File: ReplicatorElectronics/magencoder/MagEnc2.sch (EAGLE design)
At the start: 15 parts, among them IC2 AS5145

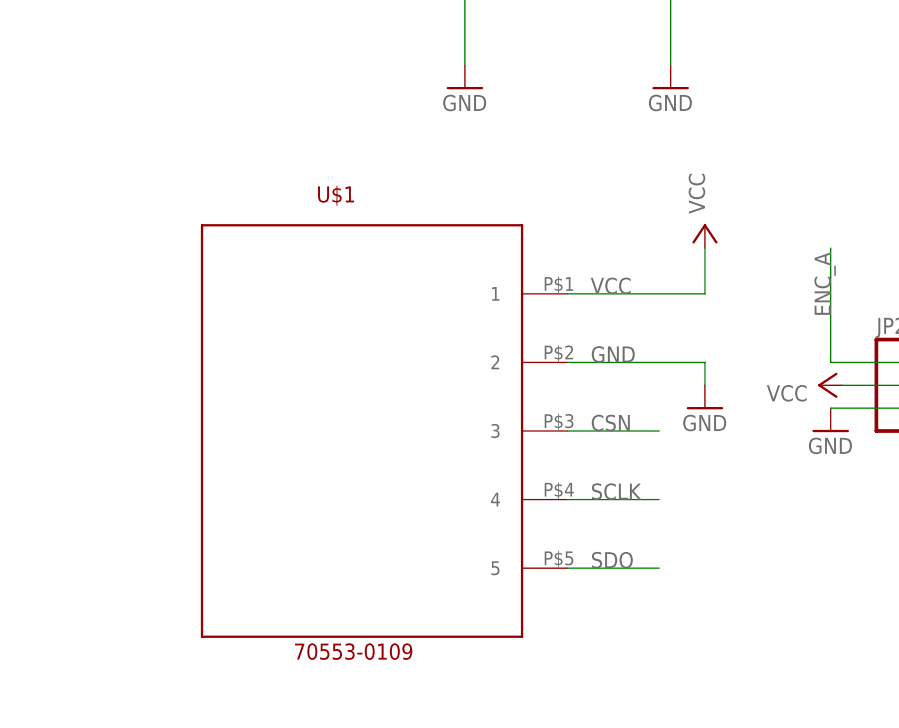
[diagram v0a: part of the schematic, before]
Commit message: 2/23/11: Added Rev. 2 Encoder Board. Fixes disconnect between layout and schematic, Header yet to be placed and routed.
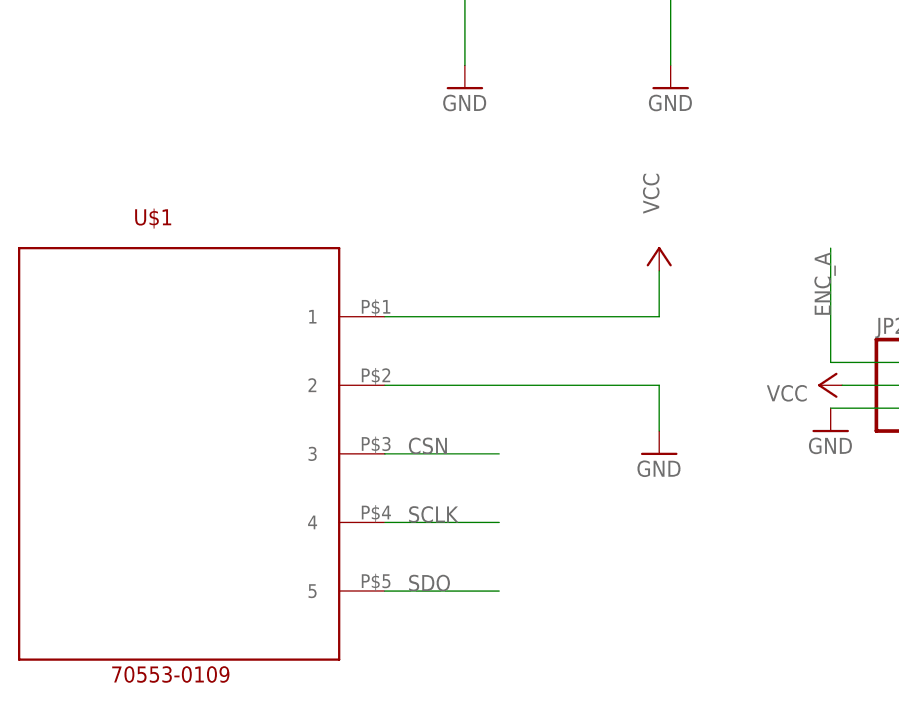
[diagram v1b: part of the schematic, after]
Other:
- moved on the sheet: U$1
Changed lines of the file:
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@@
 <part name="C2" library="rcl" deviceset="C-EU" device="C0805K" value="10uf"/>
 <part name="C4" library="rcl" deviceset="C-EU" device="C0805K" value="10uf"/>
+<part name="U$1" library="70553-0109" deviceset="70553-0106" device=""/>
 <part name="P+2" library="supply1" deviceset="VCC" device=""/>
-<part name="GND1" library="supply1" deviceset="GND" device=""/>
-<part name="U$1" library="70553-0109" deviceset="70553-0106" device=""/>
+<part name="GND7" library="supply1" deviceset="GND" device=""/>
 </parts>
 <sheets>
@@
 <instance part="C2" gate="G$1" x="123.19" y="43.18"/>
 <instance part="C4" gate="G$1" x="138.43" y="43.18"/>
-<instance part="P+2" gate="VCC" x="-17.78" y="2.54" smashed="yes">
-<attribute name="VALUE" x="-17.78" y="3.81" size="1.778" layer="96" rot="R90"/>
+<instance part="U$1" gate="G$1" x="-86.36" y="-40.64"/>
+<instance part="P+2" gate="VCC" x="-22.86" y="0" smashed="yes">
+<attribute name="VALUE" x="-22.86" y="3.81" size="1.778" layer="96" rot="R90"/>
 </instance>
-<instance part="GND1" gate="1" x="-17.78" y="-17.78"/>
-<instance part="U$1" gate="G$1" x="-66.04" y="-38.1"/>
+<instance part="GND7" gate="1" x="-22.86" y="-22.86"/>
 </instances>
 <busses>
@@
 </segment>
 <segment>
-<wire x1="-33.02" y1="-12.7" x2="-17.78" y2="-12.7" width="0.1524" layer="91"/>
-<label x="-30.48" y="-12.7" size="1.778" layer="95"/>
-<pinref part="GND1" gate="1" pin="GND"/>
-<wire x1="-17.78" y1="-12.7" x2="-17.78" y2="-15.24" width="0.1524" layer="91"/>
 <pinref part="U$1" gate="G$1" pin="2"/>
+<pinref part="GND7" gate="1" pin="GND"/>
+<wire x1="-53.34" y1="-15.24" x2="-22.86" y2="-15.24" width="0.1524" layer="91"/>
+<wire x1="-22.86" y1="-15.24" x2="-22.86" y2="-20.32" width="0.1524" layer="91"/>
 </segment>
 <segment>
@@
 </segment>
 <segment>
-<wire x1="-33.02" y1="-5.08" x2="-17.78" y2="-5.08" width="0.1524" layer="91"/>
-<label x="-30.48" y="-5.08" size="1.778" layer="95"/>
+<pinref part="U$1" gate="G$1" pin="1"/>
 <pinref part="P+2" gate="VCC" pin="VCC"/>
-<wire x1="-17.78" y1="-5.08" x2="-17.78" y2="0" width="0.1524" layer="91"/>
-<pinref part="U$1" gate="G$1" pin="1"/>
+<wire x1="-53.34" y1="-7.62" x2="-22.86" y2="-7.62" width="0.1524" layer="91"/>
+<wire x1="-22.86" y1="-7.62" x2="-22.86" y2="-2.54" width="0.1524" layer="91"/>
 </segment>
 </net>
@@
 </segment>
 </net>
+<net name="CSN" class="0">
+<segment>
+<pinref part="IC2" gate="G$1" pin="CSN"/>
+<wire x1="58.42" y1="38.1" x2="66.04" y2="38.1" width="0.1524" layer="91"/>
+<label x="58.42" y="38.1" size="1.778" layer="95"/>
+</segment>
+<segment>
+<pinref part="U$1" gate="G$1" pin="3"/>
+<wire x1="-53.34" y1="-22.86" x2="-40.64" y2="-22.86" width="0.1524" layer="91"/>
+<label x="-50.8" y="-22.86" size="1.778" layer="95"/>
+</segment>
+</net>
 <net name="SCLK" class="0">
 <segment>
@@
 </segment>
 <segment>
-<wire x1="-33.02" y1="-27.94" x2="-22.86" y2="-27.94" width="0.1524" layer="91"/>
-<label x="-30.48" y="-27.94" size="1.778" layer="95"/>
 <pinref part="U$1" gate="G$1" pin="4"/>
+<wire x1="-53.34" y1="-30.48" x2="-40.64" y2="-30.48" width="0.1524" layer="91"/>
+<label x="-50.8" y="-30.48" size="1.778" layer="95"/>
 </segment>
 </net>
@@
 </segment>
 <segment>
-<wire x1="-33.02" y1="-35.56" x2="-22.86" y2="-35.56" width="0.1524" layer="91"/>
-<label x="-30.48" y="-35.56" size="1.778" layer="95"/>
 <pinref part="U$1" gate="G$1" pin="5"/>
-</segment>
-</net>
-<net name="CSN" class="0">
-<segment>
-<pinref part="IC2" gate="G$1" pin="CSN"/>
-<wire x1="58.42" y1="38.1" x2="66.04" y2="38.1" width="0.1524" layer="91"/>
-<label x="58.42" y="38.1" size="1.778" layer="95"/>
-</segment>
-<segment>
-<wire x1="-33.02" y1="-20.32" x2="-22.86" y2="-20.32" width="0.1524" layer="91"/>
-<label x="-30.48" y="-20.32" size="1.778" layer="95"/>
-<pinref part="U$1" gate="G$1" pin="3"/>
+<wire x1="-53.34" y1="-38.1" x2="-40.64" y2="-38.1" width="0.1524" layer="91"/>
+<label x="-50.8" y="-38.1" size="1.778" layer="95"/>
 </segment>
 </net>
@@
 </sheet>
 </sheets>
-<errors>
-</errors>
 </schematic>
 </drawing>

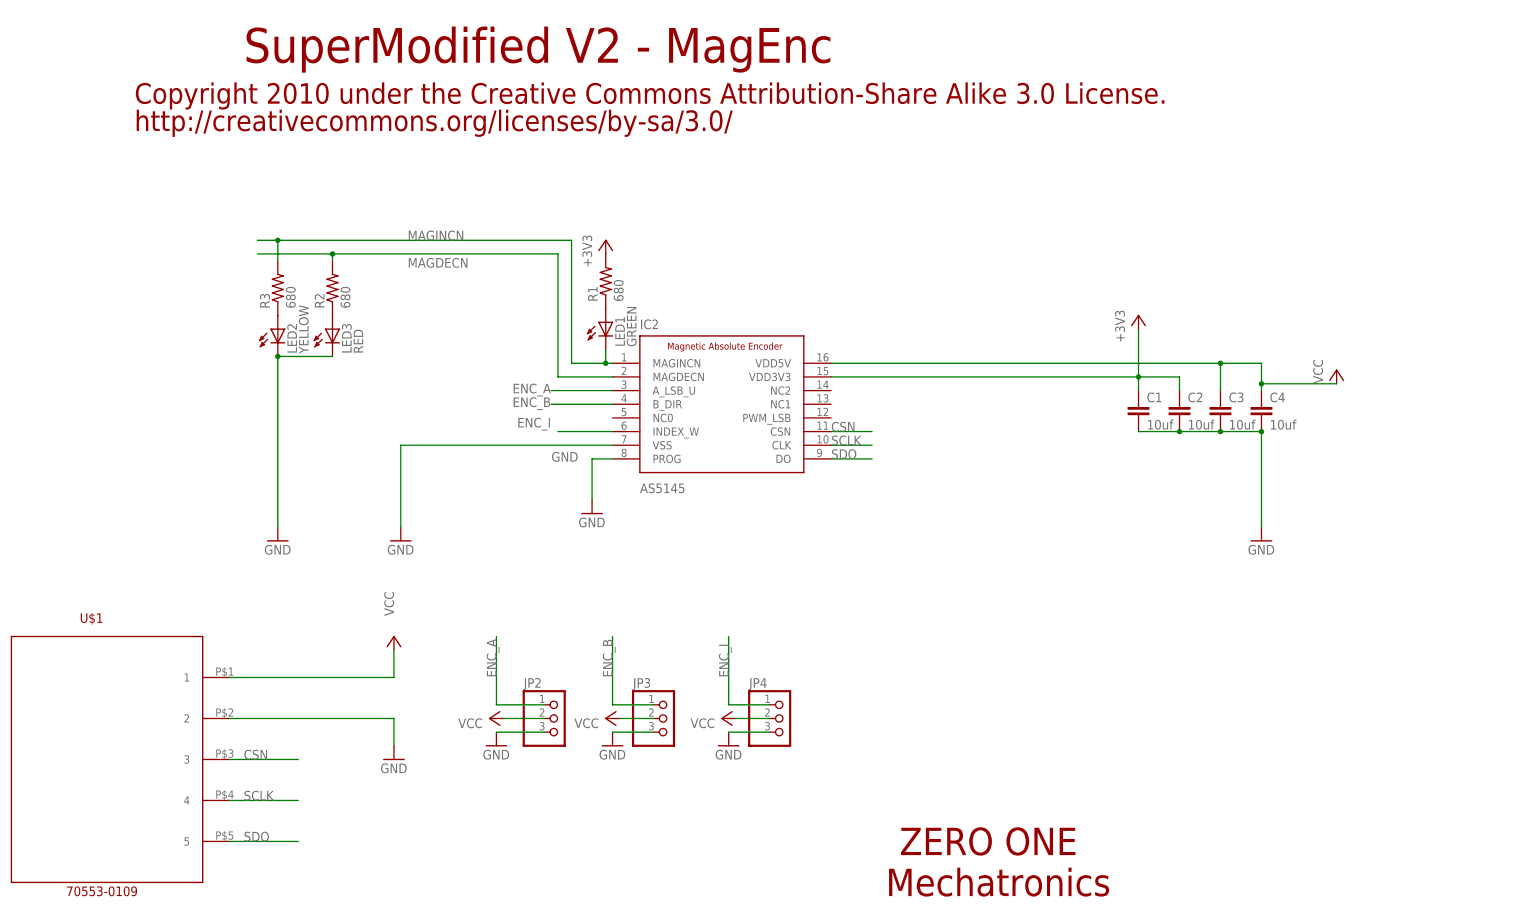
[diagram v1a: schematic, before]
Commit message: 2/23/11: Added Rev. 3 of Encoder Board. This layout is complete, pending design changes which add pass-through servo control signals.
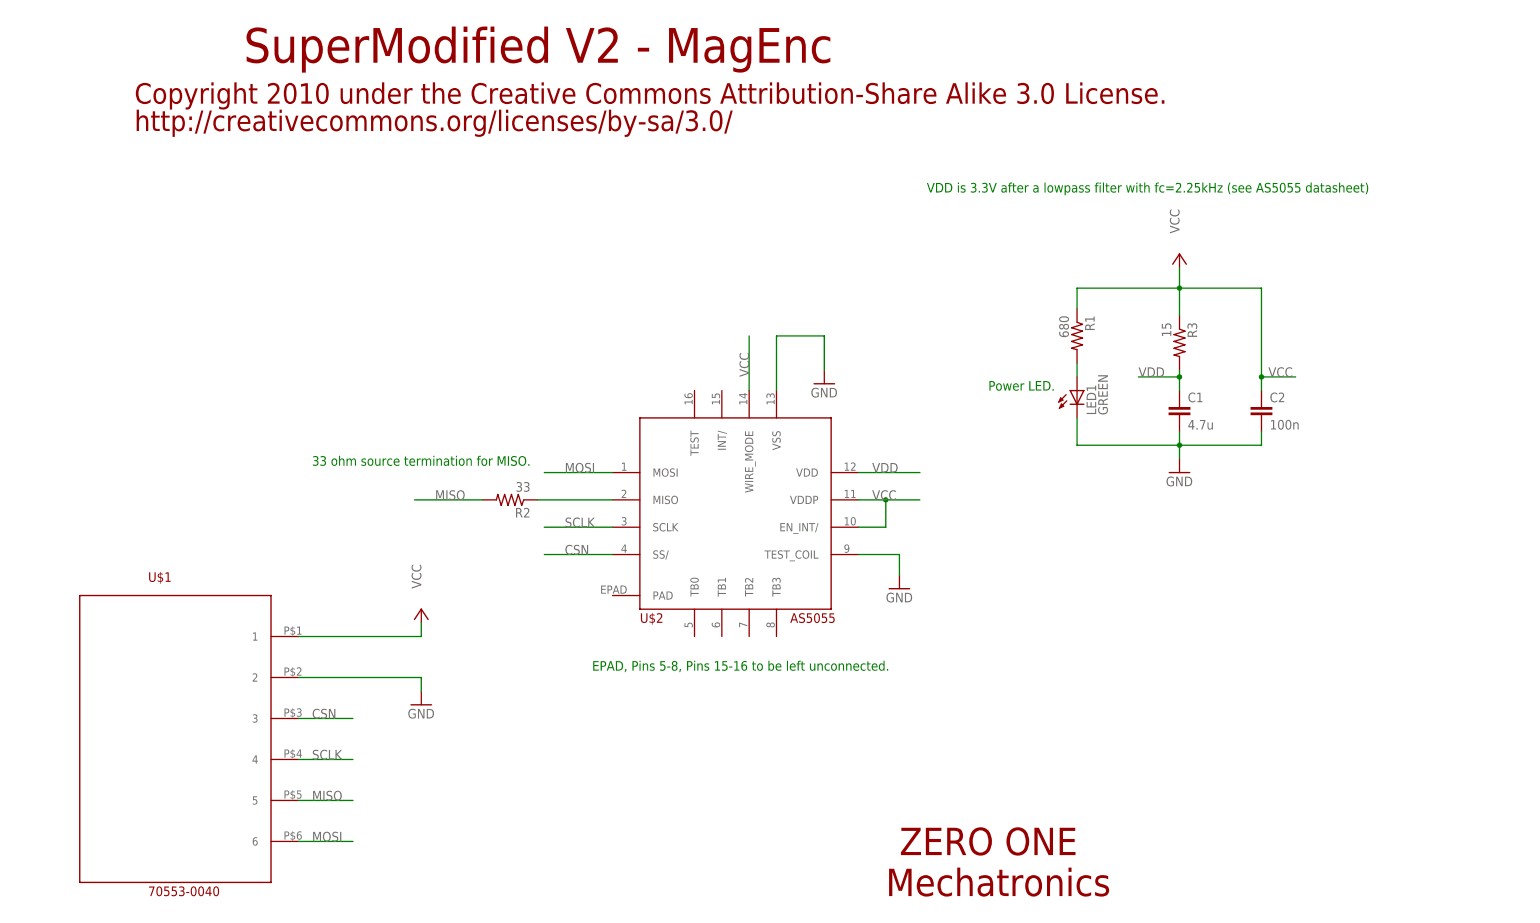
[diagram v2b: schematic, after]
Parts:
- removed C3, C4: 10uf, rcl:C-EUC0805K
- removed IC2: AS5145, zo_TMS320DMC:ADS5040
- removed JP2, JP3, JP4: (no value), pinhead:PINHD-1X3
- removed LED2: YELLOW, led:LEDCHIPLED_0805
- removed LED3: RED, led:LEDCHIPLED_0805
- added U$2: AS5055, AS5055:AS5055
- C1: value 10uf -> 4.7u
- C2: value 10uf -> 100n
- R2: value 680 -> 33
- R3: value 680 -> 15
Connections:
- removed net +3V3: C1.1, C2.1, IC2.VDD3V3, R1.2
- removed net ENC_A: IC2.A_LSB_U, JP2.1
- removed net ENC_B: IC2.B_DIR, JP3.1
- removed net ENC_I: IC2.INDEX_W, JP4.1
- removed net MAGDECN: IC2.MAGDECN, R2.2
- removed net MAGINCN: IC2.MAGINCN, LED1.C, R3.2
- removed net N$5: LED2.A, R3.1
- removed net SDO: IC2.DO, U$1.5
- new net MISO: R2.2, U$1.5
- new net MOSI: U$1.6, U$2.MOSI
- new net VDD: C1.1, R3.2, U$2.VDD
- net CSN: now also U$2.SS/; no longer IC2.CSN
- net GND: now also LED1.C, U$2.TEST_COIL, U$2.VSS; no longer C3.2, C4.2, IC2.PROG, IC2.VSS, JP2.3, JP3.3, JP4.3, LED2.C, LED3.C
- net N$1: now also R1.2; no longer R1.1
- net N$4: now also U$2.MISO; no longer LED3.A
- net SCLK: now also U$2.SCLK; no longer IC2.CLK
- net VCC: now also C2.1, R1.1, R3.1, U$2.EN_INT/, U$2.VDDP, U$2.WIRE_MODE; no longer C3.1, C4.1, IC2.VDD5V, JP2.2, JP3.2, JP4.2
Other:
- note added: "33 ohm source termination for MISO."
- note added: "EPAD, Pins 5-8, Pins 15-16 to be left unconnected."
- note added: "Power LED."
- note added: "VDD is 3.3V after a lowpass filter with fc=2.25kHz (see AS5055 datasheet)"
- moved on the sheet: C1, C2, LED1, R1, R2, R3

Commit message: 3/7/12: Rev 4 of the Encoder Board. Added feed-through for servo, may yet need layout modifications to alter placement of encoder IC or size of mounting holes.
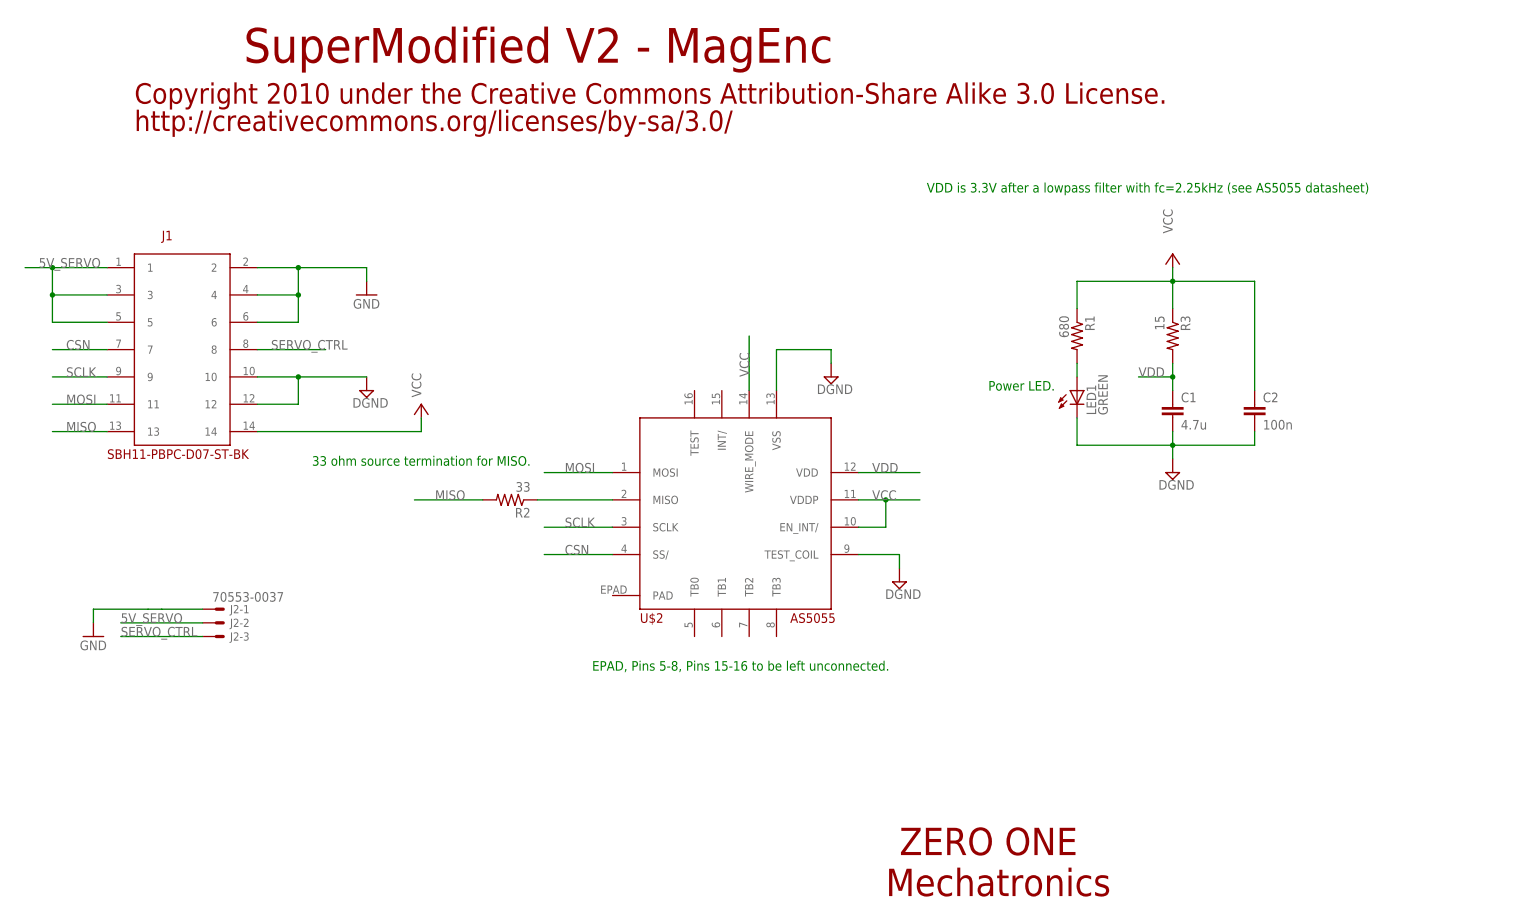
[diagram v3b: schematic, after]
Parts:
- removed U$1: 70553-0106, 70553-0109:70553-0106
- added J1: SBH11-PBPC-D07-ST-BK, SBH11-PBPC-D07-ST-BK:SBH11-PBPC-D07-ST-BK
- added J2: 70553-0037, con-molex:C-GRID-03-70553
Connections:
- new net 5V_SERVO: J1.1, J1.3, J1.5, J2-2.S
- new net DGND: C1.2, C2.2, J1.10, J1.12, LED1.C, U$2.TEST_COIL, U$2.VSS
- new net SERVO_CTRL: J1.8, J2-3.S
- net CSN: now also J1.7; no longer U$1.3
- net GND: now also J1.2, J1.4, J1.6, J2-1.S; no longer C1.2, C2.2, LED1.C, U$1.2, U$2.TEST_COIL, U$2.VSS
- net MISO: now also J1.13; no longer U$1.5
- net MOSI: now also J1.11; no longer U$1.6
- net SCLK: now also J1.9; no longer U$1.4
- net VCC: now also J1.14; no longer U$1.1
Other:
- moved on the sheet: C1, C2, R3
